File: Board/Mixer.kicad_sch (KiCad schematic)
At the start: 45 parts, among them IC26 LM3900N, J6 Conn_01x04_Pin, U6 LM386, U7 LM386, X4 1503_09

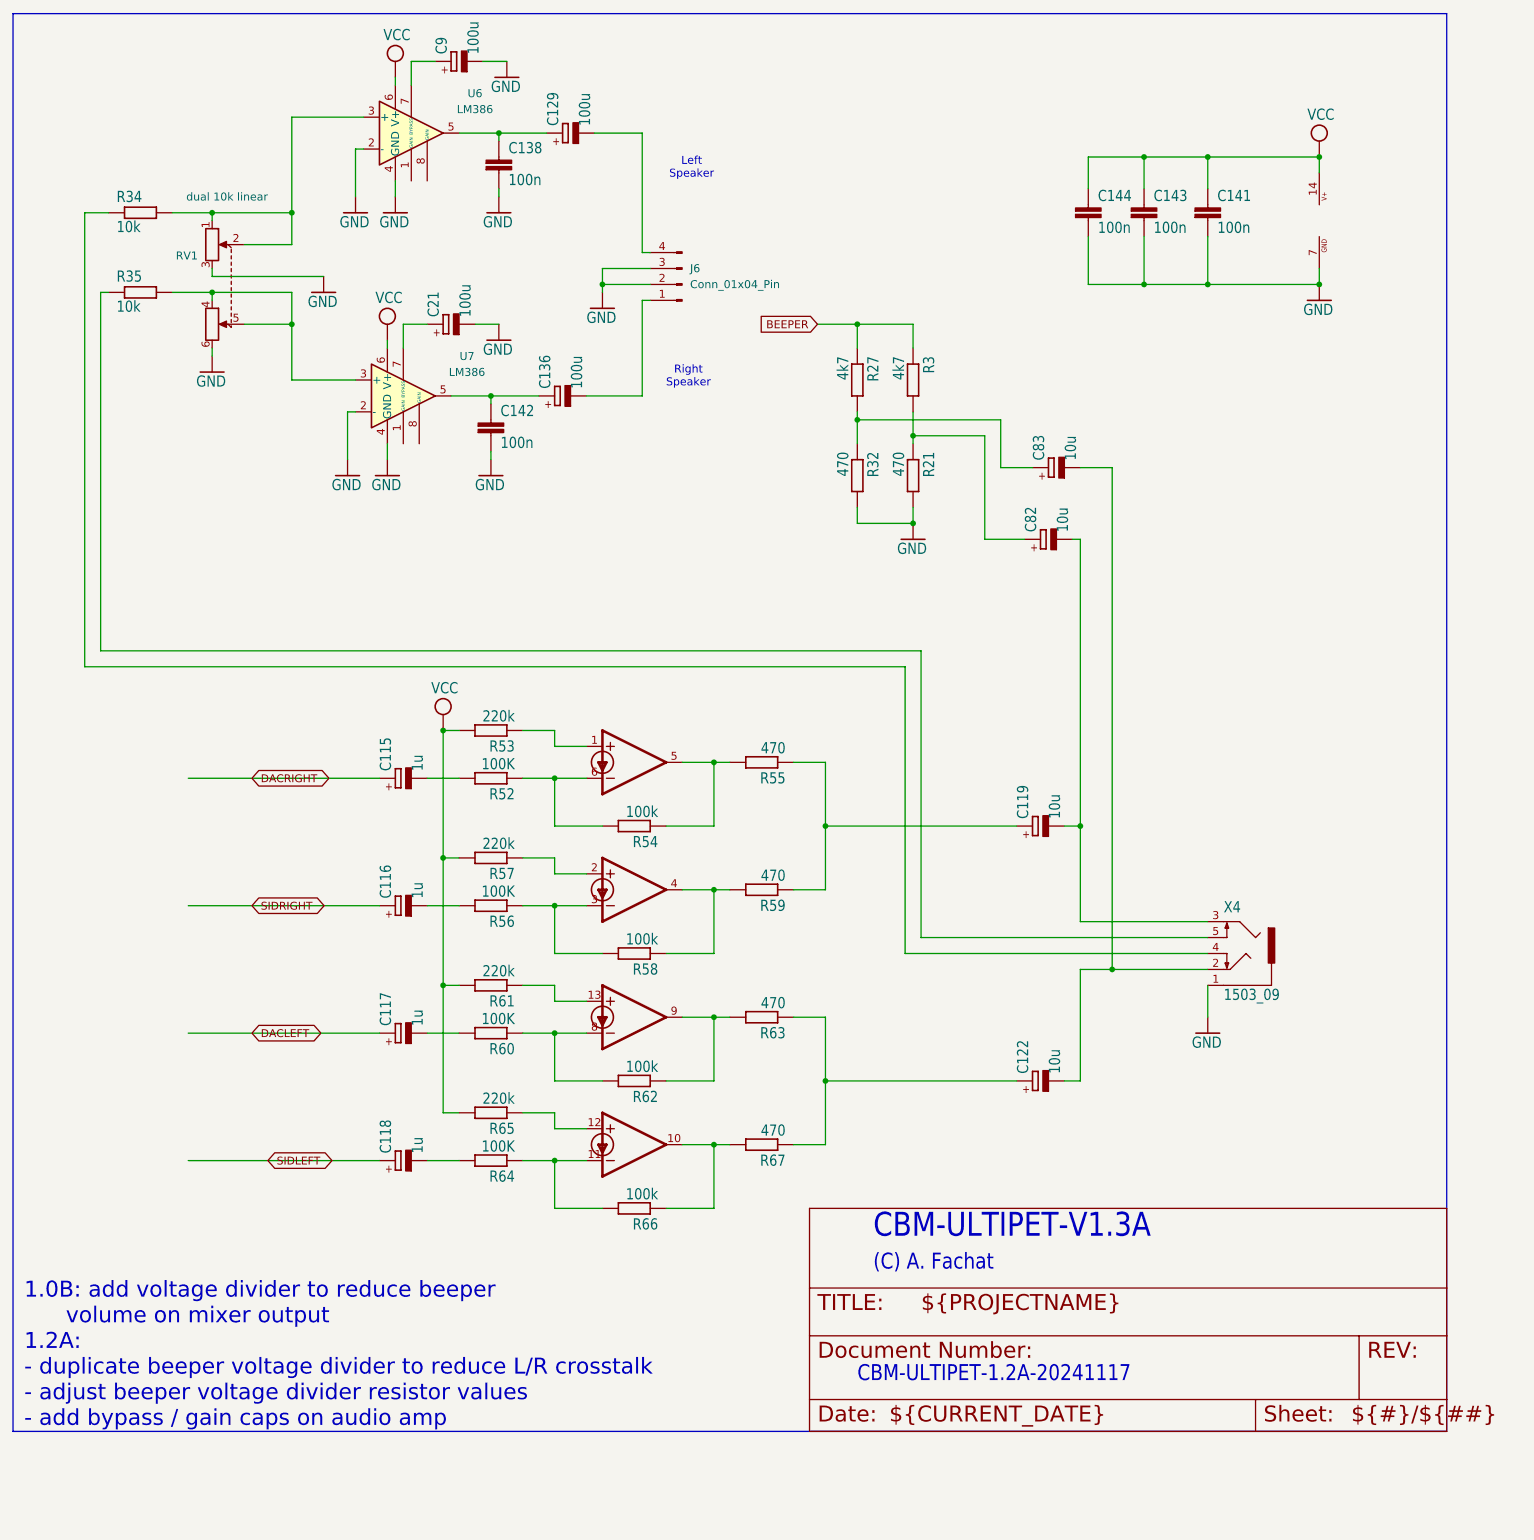
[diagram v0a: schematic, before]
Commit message: add missing chg log for mixer
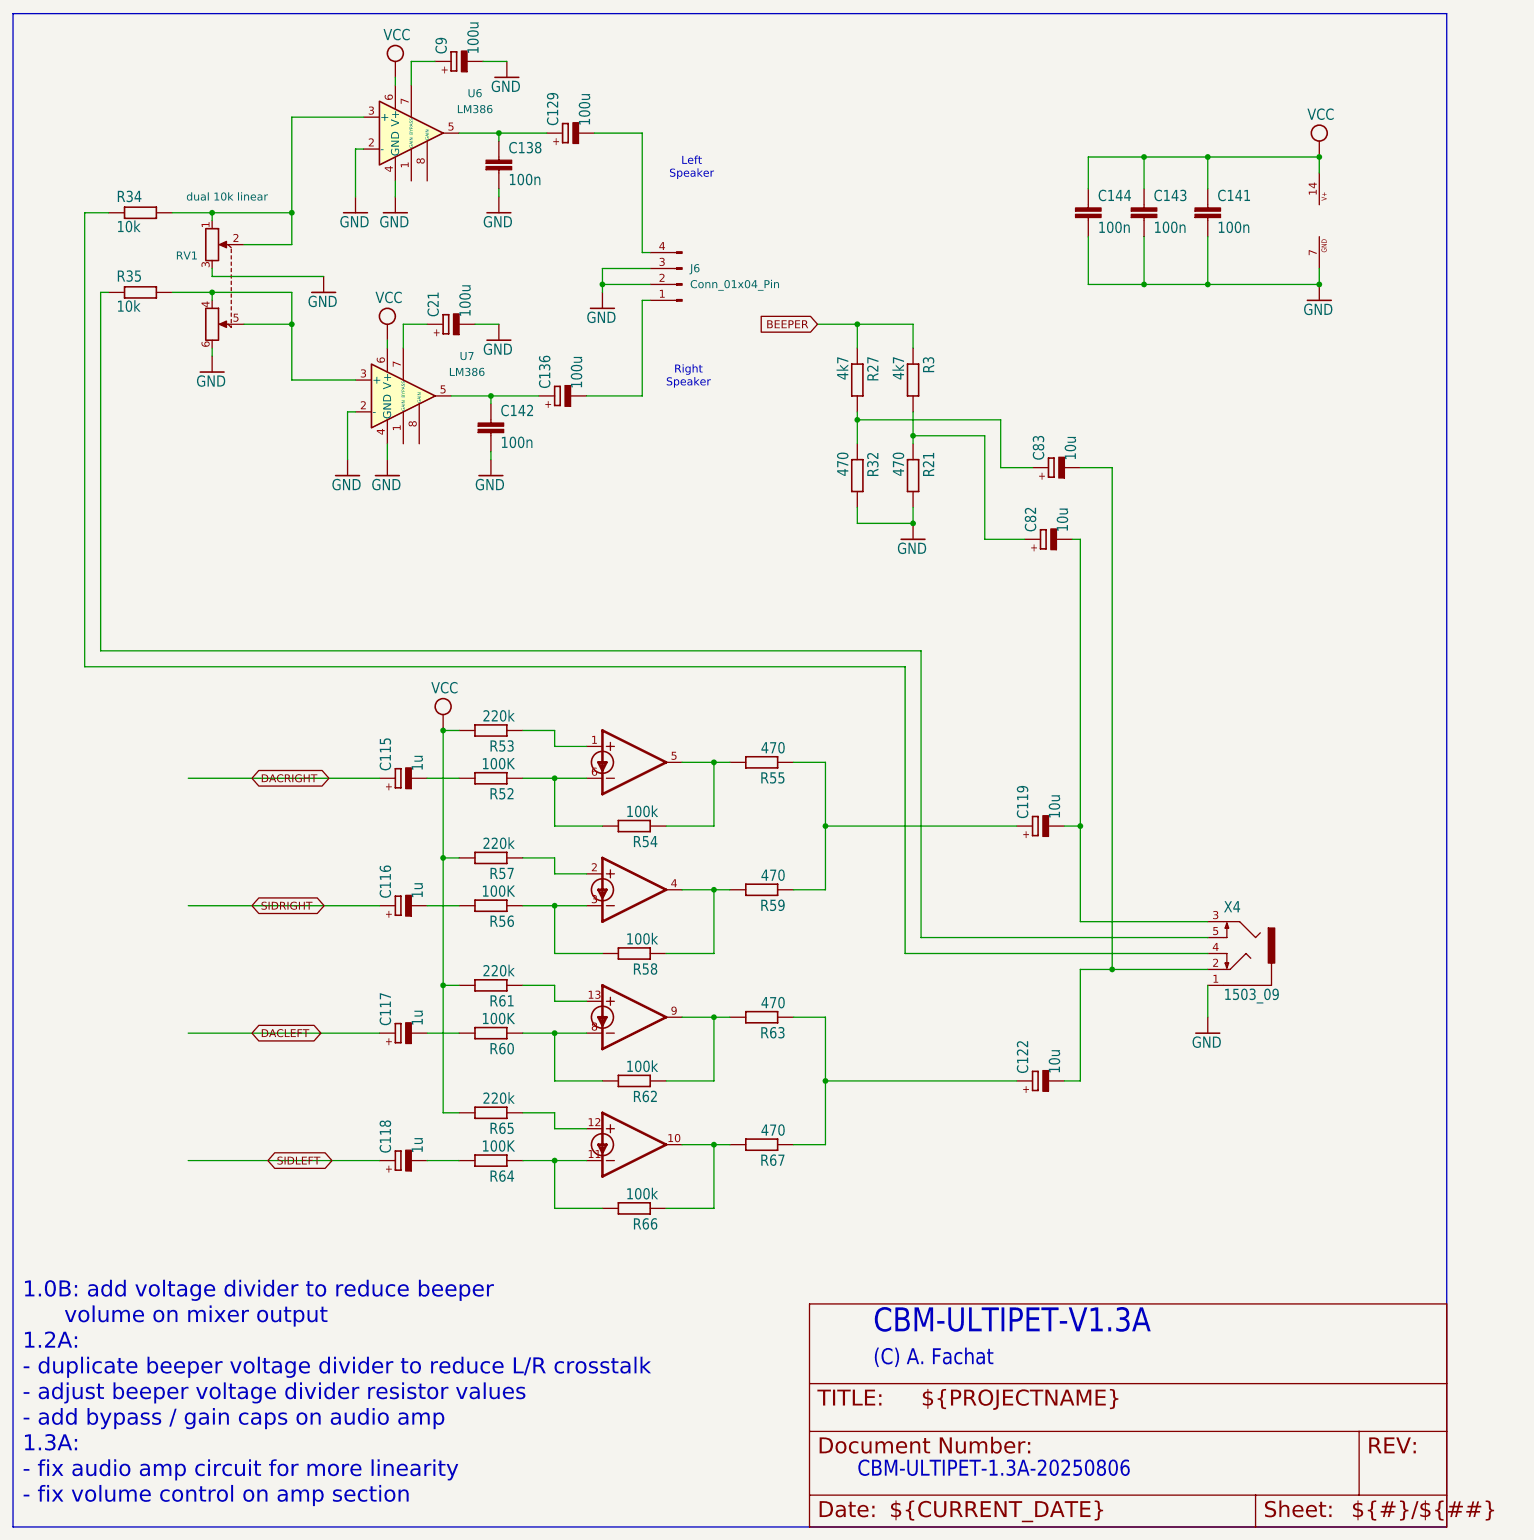
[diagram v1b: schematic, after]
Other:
- note added: "1.0B: add voltage divider to reduce beeper volume on mixer output 1.2A: - duplicate beeper voltage divider to reduce L/R crosstalk - adjust beeper voltage divider resistor values - add bypass / gain caps on audio amp 1.3A: - fix audio amp circuit for more linearity - fix volume control on amp section"
- note added: "CBM-ULTIPET-1.3A-20250806"
- note removed: "1.0B: add voltage divider to reduce beeper volume on mixer output 1.2A: - duplicate beeper voltage divider to reduce L/R crosstalk - adjust beeper voltage divider resistor values - add bypass / gain caps on audio amp"
- note removed: "CBM-ULTIPET-1.2A-20241117"
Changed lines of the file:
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@@
 	(text "CBM-ULTIPET-V1.3A"
 		(exclude_from_sim no)
-		(at 167.64 213.36 0)
+		(at 167.64 228.6 0)
 		(effects
 			(font
@@
 	(text "(C) A. Fachat"
 		(exclude_from_sim no)
-		(at 167.64 218.44 0)
+		(at 167.64 233.68 0)
 		(effects
 			(font
@@
 		)
 	)
-	(text "CBM-ULTIPET-1.2A-20241117\n"
+	(text "CBM-ULTIPET-1.3A-20250806\n"
 		(exclude_from_sim no)
-		(at 165.1 236.22 0)
+		(at 165.1 251.46 0)
 		(effects
 			(font
@@
 		)
 	)
-	(text "1.0B: add voltage divider to reduce beeper \n      volume on mixer output\n1.2A: \n- duplicate beeper voltage divider to reduce L/R crosstalk\n- adjust beeper voltage divider resistor values\n- add bypass / gain caps on audio amp"
+	(text "1.0B: add voltage divider to reduce beeper \n      volume on mixer output\n1.2A: \n- duplicate beeper voltage divider to reduce L/R crosstalk\n- adjust beeper voltage divider resistor values\n- add bypass / gain caps on audio amp\n1.3A:\n- fix audio amp circuit for more linearity\n- fix volume control on amp section"
 		(exclude_from_sim no)
-		(at 32.258 231.648 0)
+		(at 32.004 237.744 0)
 		(effects
 			(font
@@
 	(polyline
 		(pts
-			(xy 30.48 17.78) (xy 30.48 243.84)
+			(xy 30.48 17.78) (xy 30.48 259.08)
 		)
 		(stroke
@@
 	(polyline
 		(pts
-			(xy 30.48 243.84) (xy 259.08 243.84)
+			(xy 30.48 259.08) (xy 259.08 259.08)
 		)
 		(stroke
@@
 	(polyline
 		(pts
-			(xy 259.08 243.84) (xy 259.08 17.78)
+			(xy 259.08 259.08) (xy 259.08 17.78)
 		)
 		(stroke
@@
 	(symbol
 		(lib_id "cbm_ultipet_v1-eagle-import:DOCFIELD")
-		(at 157.48 243.84 0)
+		(at 157.48 259.08 0)
 		(unit 1)
 		(exclude_from_sim no)
@@
 		(dnp no)
 		(property "Reference" "#FRAME10"
-			(at 157.48 243.84 0)
+			(at 157.48 259.08 0)
 			(effects
 				(font
@@
 		)
 		(property "Value" "DOCFIELD"
-			(at 157.48 243.84 0)
+			(at 157.48 259.08 0)
 			(effects
 				(font
@@
 		)
 		(property "Footprint" ""
-			(at 157.48 243.84 0)
+			(at 157.48 259.08 0)
 			(effects
 				(font
@@
 		)
 		(property "Datasheet" ""
-			(at 157.48 243.84 0)
+			(at 157.48 259.08 0)
 			(effects
 				(font
@@
 		)
 		(property "Description" ""
-			(at 157.48 243.84 0)
+			(at 157.48 259.08 0)
 			(effects
 				(font
